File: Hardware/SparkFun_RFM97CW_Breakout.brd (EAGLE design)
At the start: 22.9 x 34.3 mm, 45 parts, among them J7 U.FL, U4 RFM97CW

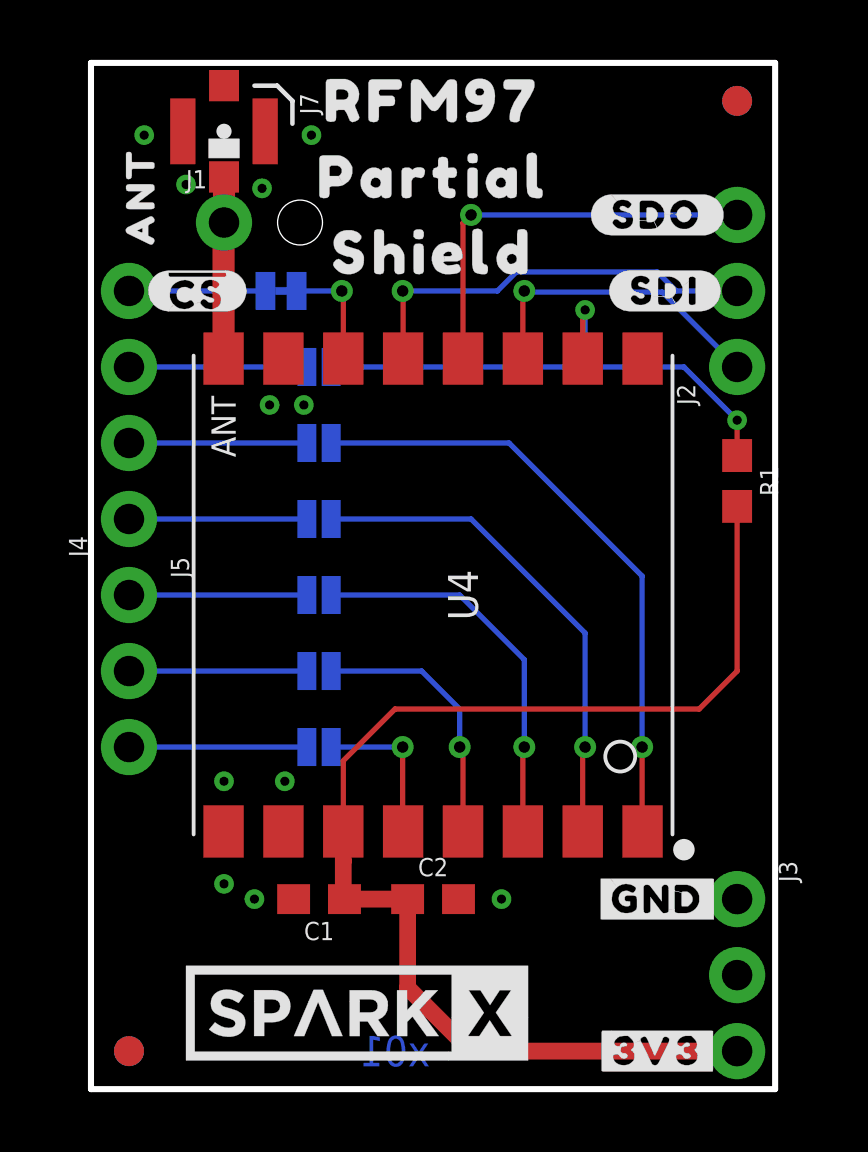
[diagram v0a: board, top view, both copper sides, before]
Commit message: Adding panel for x02
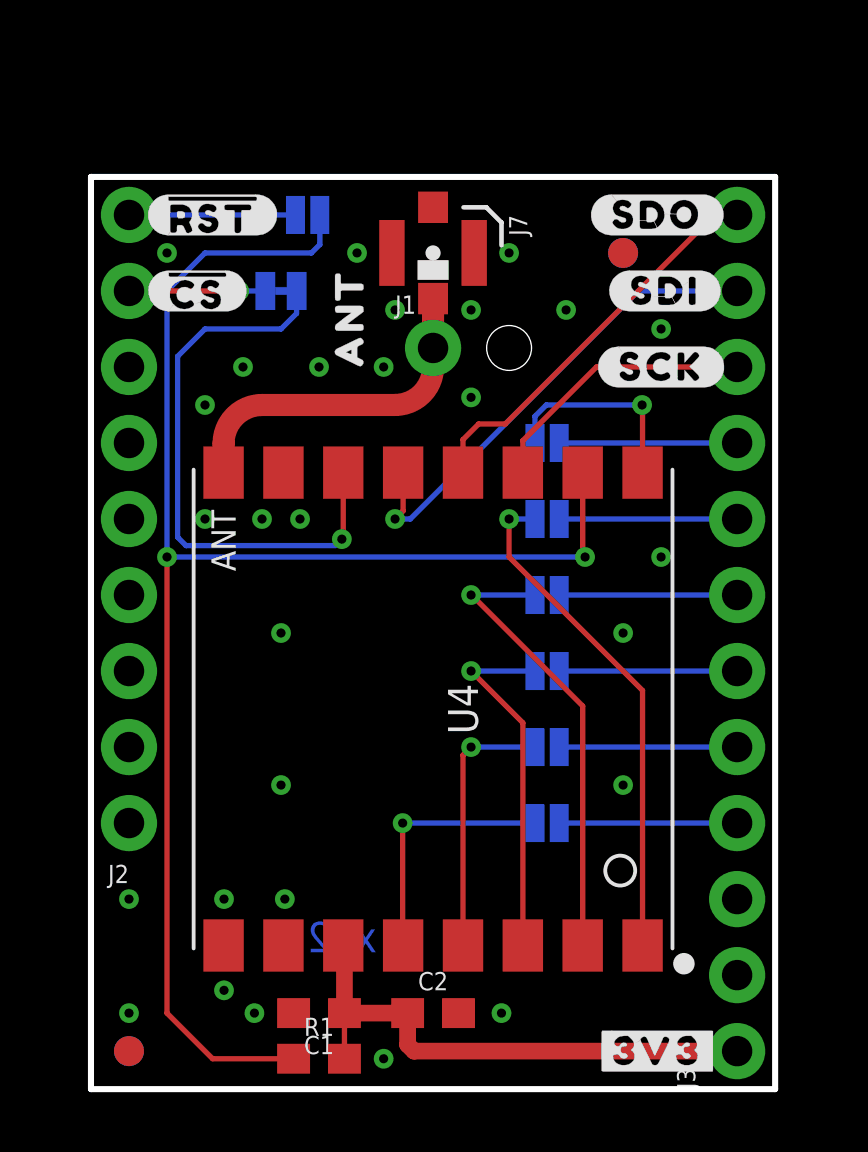
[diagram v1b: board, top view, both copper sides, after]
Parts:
- removed J4: (no value), SparkFun-Connectors:1X04_NO_SILK
- removed J5: (no value), SparkFun-Connectors:1X03_NO_SILK
- removed JP8: JUMPER-SMT_2_NO_NO-SILK, SparkFun-Jumpers:SMT-JUMPER_2_NO_NO-SILK
- removed U$14: (no value), output:#DIO2#3
- removed U$15: (no value), output:#DIO3#2
- removed U$16: (no value), output:#DIO4#1
- removed U$18: (no value), output:PARTIAL1
- added JP0, JP1: JUMPER-SMT_2_NO_NO-SILK, SparkFun-Jumpers:SMT-JUMPER_2_NO_NO-SILK
- added U$23: (no value), output:#DIO0#0
- added U$24: (no value), output:#DIO1#0
- added U$25: (no value), output:#DIO2#0
- added U$26: (no value), output:#DIO3#0
- added U$27: (no value), output:#DIO4#0
- added U$28: (no value), output:#DIO5#0
- J2: device SparkFun-Connectors:1X03_NO_SILK -> SparkFun-Connectors:1X09_NO_SILK
- J3: device SparkFun-Connectors:1X03_NO_SILK -> SparkFun-Connectors:1X12_NO_SILK
- JP2: value JUMPER-SMT_2_NC_TRACE_NO-SILK -> JUMPER-SMT_2_NO_NO-SILK; device SparkFun-Jumpers:SMT-JUMPER_2_NC_TRACE_NO-SILK -> SparkFun-Jumpers:SMT-JUMPER_2_NO_NO-SILK
- JP7: value JUMPER-SMT_2_NO_NO-SILK -> JUMPER-SMT_2_NC_TRACE_NO-SILK; device SparkFun-Jumpers:SMT-JUMPER_2_NO_NO-SILK -> SparkFun-Jumpers:SMT-JUMPER_2_NC_TRACE_NO-SILK
- U$11: device output:#GND#1 -> output:MINI0
- U$12: device output:#DIO0#5 -> output:#SCK#0
- U$13: device output:#DIO1#4 -> output:##RST##0
- U$5: device output:#SCK#2 -> output:#SCK#0
- moved J2 25.4 mm to (1.27, 8.89)
- moved R1 23.8 mm to (7.62, 1.02), turned to 0 degrees
- moved U$12 19.5 mm to (19.1, 24.1)
- moved U$22 17.8 mm to (8.38, 20.3), flipped to the bottom
- moved U$19 16.8 mm to (8.38, 16.5), flipped to the bottom
- moved U$20 16.8 mm to (8.38, 11.4), flipped to the bottom
- moved JP2 15.5 mm to (15.2, 14.0), turned to 180 degrees
- moved JP6 15.2 mm to (7.24, 29.2)
- moved U$13 15.2 mm to (4.06, 29.2), flipped to the top
- moved U$11 13.0 mm to (8.38, 14.0), flipped to the bottom
- moved JP3 10.8 mm to (15.2, 16.5), turned to 180 degrees
- moved JP7 10.2 mm to (6.35, 26.7)
- moved J1 8.15 mm to (11.4, 24.8)
- moved U$1 8.08 mm to (8.64, 25.8)
- moved J7 8.08 mm to (11.4, 27.9)
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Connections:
- removed net N$10: J5.1, JP7.2
- removed net N$9: J5.2, JP6.2
- new net N$4: J3.5, JP1.2
- new net N$5: J3.4, JP0.2
- new net N$6: J3.7, JP3.2
- net !CS!: now also JP7.1; no longer JP2.1
- net !RST!: now also JP6.1; no longer JP3.1
- net 3.3V: now also J3.1; no longer J3.3
- net DIO0: now also JP0.1; no longer JP8.1
- net DIO1: now also JP1.1; no longer JP6.1
- net DIO2: now also JP2.1; no longer JP7.1
- net DIO3: now also JP3.1; no longer JP5.1
- net DIO5: now also JP5.1
- net GND: now also J3.3; no longer J3.1
- net N$1: now also J3.6, JP2.2; no longer J5.3, JP8.2
- net N$2: now also J2.9, JP6.2; no longer J4.4, JP2.2
- net N$3: now also J2.8, JP7.2; no longer J4.3, JP3.2
- net N$7: now also J3.8; no longer J4.2
- net N$8: now also J3.9; no longer J4.1
- net SCK: now also J3.10; no longer J2.1
- net SDI: now also J3.11; no longer J2.2
- net SDO: now also J3.12; no longer J2.3
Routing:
- net !RST!: track 19.0 -> 52.6 mm
- net 3.3V: track 42.5 -> 18.1 mm
- net !CS!: track 3.79 -> 19.3 mm
- net DIO5: track 0.00 -> 6.89 mm, vias 0 -> 1
- net N$9: track 5.94 -> 0.00 mm
- net N$6: track 0.00 -> 5.94 mm
- net N$5: track 0.00 -> 5.94 mm
- net N$4: track 0.00 -> 5.94 mm
- net N$10: track 5.94 -> 0.00 mm
- net ANT: track 6.08 -> 11.3 mm
- net DIO4: track 20.8 -> 17.0 mm
- net DIO0: track 5.21 -> 8.52 mm
- net SDI: track 14.0 -> 16.2 mm
- net N$3: track 5.94 -> 4.56 mm, vias 0 -> 1
- net DIO3: track 16.7 -> 15.4 mm
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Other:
- board size 22.9 x 34.3 mm -> 22.9 x 30.5 mm
- board text added: "x02"
- board text removed: "x01"
